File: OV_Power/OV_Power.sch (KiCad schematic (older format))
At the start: 44 parts, among them J4 SpadeLug, J5 SpadeLug, Q1 SSM3K341R, Q2 2N7002BK, U1 LT3796, U2 LT1936

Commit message: Changing connectors again, also fixed a library fubar...
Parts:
- L1: symbol OV_Power-rescue:MSD1260-333-F_inductors-OV_Power-rescue -> OpenVent:MSD1260-333
- U1: symbol OV_Power-rescue:LT3796-F_ICs -> OpenVent:LT3796
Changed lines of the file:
@@
 $EndComp
 $Comp
-L OV_Power-rescue:LT3796-F_ICs U1
+L OpenVent:LT3796 U1
 U 1 1 5FAE7EAD
 P 4100 3800
@@
 $EndComp
 $Comp
-L OV_Power-rescue:MSD1260-333-F_inductors-OV_Power-rescue L1
+L OpenVent:MSD1260-333 L1
 U 1 1 5FB0C2C0
 P 5400 1050
@@
 $EndComp
 $Comp
-L OV_Power-rescue:MSD1260-333-F_inductors-OV_Power-rescue L1
+L OpenVent:MSD1260-333 L1
 U 2 1 5FB0D579
 P 6350 1300

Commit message: Added 3 pin JST 10amp connector for the battery.  Now all we have to worry about is connecting the wiring harness to the battery correctly...
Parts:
- removed J4: SpadeLug, F_Connectors:TE_1217861-1, symbol OV_Power-rescue:SpadeLug-F_connectors
- removed J5: SpadeLug, F_Connectors:TE_1217861-1, symbol OV_Power-rescue:SpadeLug-F_connectors-OV_Power-rescue
- added J4: Conn_01x03_JST_B3P_Vert, F_Connectors:JST_B3P-VH(LF)(SN), symbol OpenVent:Conn_01x03_JST_B3P_Vert
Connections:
- wire segments 159 -> 161
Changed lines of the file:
@@
 L OV_Power-rescue:GND-OpenVent #PWR015
 U 1 1 5F957C60
-P 10450 1550
-F 0 "#PWR015" H 10450 1300 50  0001 C CNN
-F 1 "GND" H 10450 1400 50  0001 C CNN
-F 2 "" H 10450 1550 50  0001 C CNN
-F 3 "" H 10450 1550 50  0001 C CNN
-	1    10450 1550
+P 10450 1250
+F 0 "#PWR015" H 10450 1000 50  0001 C CNN
+F 1 "GND" H 10450 1100 50  0001 C CNN
+F 2 "" H 10450 1250 50  0001 C CNN
+F 3 "" H 10450 1250 50  0001 C CNN
+	1    10450 1250
 	1    0    0    -1
 $EndComp
@@
 	3950 5450 3650 5450
 Connection ~ 3950 5450
-Text Notes 10250 2550 0    50   ~ 0
+Text Notes 10200 1950 0    50   ~ 0
 NEED CONNECTOR\nDEFINITION FOR\nGELL CELL.\nTHIS CONNECTION\nALSO NEEDS TO\nBE FUSED.
 $Comp
@@
 Wire Wire Line
 	8750 1050 9100 1050
-$Comp
-L OV_Power-rescue:SpadeLug-F_connectors J4
-U 1 1 5FCBB8E9
-P 10750 1050
-F 0 "J4" H 10780 1096 50  0000 L CNN
-F 1 "SpadeLug" H 10780 1005 50  0000 L CNN
-F 2 "F_Connectors:TE_1217861-1" H 10750 1050 50  0001 L BNN
-F 3 "https://www.te.com/commerce/DocumentDelivery/DDEController?Action=srchrtrv&DocNm=1217861&DocType=Customer+Drawing&DocLang=English" H 10750 1050 50  0001 L BNN
-F 4 "TE Connectivity AMP Connectors" H 10750 1050 50  0001 L BNN "Mfr"
-F 5 "1217861-1" H 10750 1050 50  0001 L BNN "MfrPn"
-F 6 "A100452CT-ND" H 10750 1050 50  0001 L BNN "DK_pn"
-F 7 "CONN QC TAB 0.250 SOLDER" H 10750 1050 50  0001 L BNN "Desc"
-F 8 "0.250\" (6.35mm) Quick Connect Male  Solder Connector Non-Insulated" H 10750 1050 50  0001 L BNN "Detailed"
-F 9 "1217861-1" H 10750 1050 50  0001 C CNN "Mfr_PN"
-	1    10750 1050
-	1    0    0    -1
-$EndComp
-$Comp
-L OV_Power-rescue:SpadeLug-F_connectors-OV_Power-rescue J5
-U 1 1 5FCBC350
-P 10750 1450
-F 0 "J5" H 10780 1496 50  0000 L CNN
-F 1 "SpadeLug" H 10780 1405 50  0000 L CNN
-F 2 "F_Connectors:TE_1217861-1" H 10750 1450 50  0001 L BNN
-F 3 "https://www.te.com/commerce/DocumentDelivery/DDEController?Action=srchrtrv&DocNm=1217861&DocType=Customer+Drawing&DocLang=English" H 10750 1450 50  0001 L BNN
-F 4 "TE Connectivity AMP Connectors" H 10750 1450 50  0001 L BNN "Mfr"
-F 5 "1217861-1" H 10750 1450 50  0001 L BNN "MfrPn"
-F 6 "A100452CT-ND" H 10750 1450 50  0001 L BNN "DK_pn"
-F 7 "CONN QC TAB 0.250 SOLDER" H 10750 1450 50  0001 L BNN "Desc"
-F 8 "0.250\" (6.35mm) Quick Connect Male  Solder Connector Non-Insulated" H 10750 1450 50  0001 L BNN "Detailed"
-F 9 "1217861-1" H 10750 1450 50  0001 C CNN "Mfr_PN"
-	1    10750 1450
-	1    0    0    -1
-$EndComp
-Wire Wire Line
-	10550 1450 10450 1450
-Wire Wire Line
-	10450 1450 10450 1550
+Wire Wire Line
+	10550 1150 10450 1150
+Wire Wire Line
+	10450 1150 10450 1250
 $Comp
 L OV_Power-rescue:Polyfuse_10A-OpenVent F1
@@
 ISP_N
 Connection ~ 6200 2300
+$Comp
+L OpenVent:Conn_01x03_JST_B3P_Vert J4
+U 1 1 5FFB3878
+P 10750 1050
+F 0 "J4" H 10830 1046 50  0000 L CNN
+F 1 "Conn_01x03_JST_B3P_Vert" H 10830 1001 50  0001 L CNN
+F 2 "F_Connectors:JST_B3P-VH(LF)(SN)" H 10750 1050 50  0001 C CNN
+F 3 "http://www.jst-mfg.com/product/pdf/eng/eVH.pdf" H 10750 1050 50  0001 C CNN
+F 4 "JST Sales America Inc." H 10750 1050 50  0001 C CNN "Mfr"
+F 5 "B3P-VH(LF)(SN)" H 10750 1050 50  0001 C CNN "Mfr_PN"
+F 6 "CONN HEADER VERT 3POS 3.96MM" H 10750 1050 50  0001 C CNN "Desc"
+F 7 "Connector Header Through Hole 3 position 0.156\" (3.96mm)" H 10750 1050 50  0001 C CNN "Detailed"
+	1    10750 1050
+	1    0    0    -1
+$EndComp
+Wire Wire Line
+	10550 950  10450 950
+Wire Wire Line
+	10450 950  10450 1150
+Connection ~ 10450 1150
 $EndSCHEMATC

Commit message: updated notes
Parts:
- J4: symbol OpenVent:Conn_01x03_JST_B3P_Vert -> OV_Power-rescue:Conn_01x03_JST_B3P_Vert-OpenVent
- L1: symbol OpenVent:MSD1260-333 -> OV_Power-rescue:MSD1260-333-OpenVent
- U1: symbol OpenVent:LT3796 -> OV_Power-rescue:LT3796-OpenVent
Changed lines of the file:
@@
 $EndComp
 $Comp
-L OpenVent:LT3796 U1
+L OV_Power-rescue:LT3796-OpenVent U1
 U 1 1 5FAE7EAD
 P 4100 3800
@@
 $EndComp
 $Comp
-L OpenVent:MSD1260-333 L1
+L OV_Power-rescue:MSD1260-333-OpenVent L1
 U 1 1 5FB0C2C0
 P 5400 1050
@@
 $EndComp
 $Comp
-L OpenVent:MSD1260-333 L1
+L OV_Power-rescue:MSD1260-333-OpenVent L1
 U 2 1 5FB0D579
 P 6350 1300
@@
 Connection ~ 6200 2300
 $Comp
-L OpenVent:Conn_01x03_JST_B3P_Vert J4
+L OV_Power-rescue:Conn_01x03_JST_B3P_Vert-OpenVent J4
 U 1 1 5FFB3878
 P 10750 1050

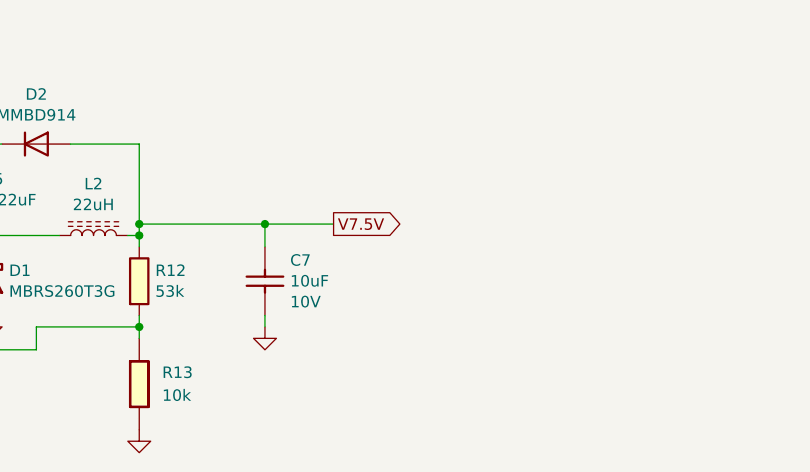
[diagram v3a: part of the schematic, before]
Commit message: Add 470 pF capacitor from U2 pin 5 to ground Add 100 nF cap to each LED, D4 to D11
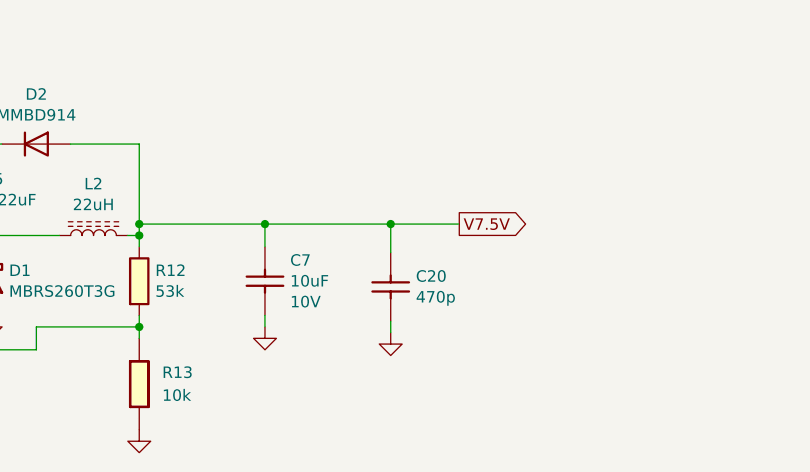
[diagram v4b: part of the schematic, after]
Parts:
- added C20: 470pF_0603_Ceramic_Capacitor,_10%,_50V,_X7R--Open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, symbol OV_Power-rescue:470pF_0603_Ceramic_Capacitor,_10%,_50V,_X7R--OpenVent_copy
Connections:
- net GND: now also C20.2
- net V7.5V: now also C20.1
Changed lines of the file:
@@
 Wire Wire Line
 	4300 5600 4350 5600
-Text GLabel 6950 5400 2    50   Output ~ 0
+Text GLabel 7500 5400 2    50   Output ~ 0
 V7.5V
-Wire Wire Line
-	6950 5400 6650 5400
 Connection ~ 6100 5400
 Wire Wire Line
@@
 	10450 950  10450 1150
 Connection ~ 10450 1150
+$Comp
+L OV_Power-rescue:470pF_0603_Ceramic_Capacitor,_10%,_50V,_X7R--OpenVent_copy C20
+U 1 1 60549715
+P 7300 5625
+F 0 "C20" V 7304 5635 50  0000 L CNN
+F 1 "470pF_0603_Ceramic_Capacitor,_10%,_50V,_X7R--OpenVent_copy" H 6575 6025 50  0001 C CNN
+F 2 "" H 7300 5625 50  0001 C CNN
+F 3 "" H 7300 5625 50  0001 C CNN
+F 4 "470p" V 7395 5635 50  0000 L CNN "Val"
+F 5 "50V" H 7275 5200 50  0001 C CNN "Voltage"
+F 6 "10%" H 7300 5625 50  0001 C CNN "Tolerance"
+	1    7300 5625
+	0    1    1    0
+$EndComp
+$Comp
+L OV_Power-rescue:GND-OpenVent #PWR016
+U 1 1 6055AEEE
+P 7200 5875
+F 0 "#PWR016" H 7200 5625 50  0001 C CNN
+F 1 "GND" H 7200 5725 50  0001 C CNN
+F 2 "" H 7200 5875 50  0001 C CNN
+F 3 "" H 7200 5875 50  0001 C CNN
+	1    7200 5875
+	1    0    0    -1
+$EndComp
+Wire Wire Line
+	6650 5400 7200 5400
+Wire Wire Line
+	7200 5525 7200 5400
+Connection ~ 7200 5400
+Wire Wire Line
+	7200 5400 7500 5400
+Wire Wire Line
+	7200 5875 7200 5825
 $EndSCHEMATC
